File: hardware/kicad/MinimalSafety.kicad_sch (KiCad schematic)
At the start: 18 parts, among them U1 TPS3431SDRBR, U11 DRV8803PWPR, U2 SN74HCS74D, U6 SN74HCS11D

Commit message: WIP: publish current unfinished CAD sources
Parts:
- removed C1, C2, C6: 100n 16V X7R, Sirokko_TFT_Passives:C_Murata_GRM188_1608_Reflow, symbol Device:C
- removed R18, R19: 10k 1%, Resistor_SMD:R_0603_1608Metric, symbol Device:R
- removed R700, R9: 10k, Resistor_THT:R_Axial_DIN0207_L6.3mm_D2.5mm_P10.16mm_Horizontal, symbol Device:R
- removed R88: 4k7 DRV_IN3_PULLDOWN, Resistor_THT:R_Axial_DIN0207_L6.3mm_D2.5mm_P10.16mm_Horizontal, symbol Device:R
- removed R89: 10k RELAY_DRIVER_OK_PULLUP, Resistor_THT:R_Axial_DIN0207_L6.3mm_D2.5mm_P10.16mm_Horizontal, symbol Device:R
- removed U1: TPS3431SDRBR, Sirokko_Safety:TPS3431_DRB0008A_3D, symbol Sirokko_Safety:TPS3431SDRBR
- removed U2: SN74HCS74D, Package_SO:SOIC-14_3.9x8.7mm_P1.27mm, symbol Sirokko_Safety:SN74HCS74D
- removed U6: SN74HCS11D, Package_SO:SOIC-14_3.9x8.7mm_P1.27mm, symbol Sirokko_Safety:SN74HCS11D
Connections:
- net RELAY_DISABLE is gone; now on net GND: U11.8 (~{ENBL})
- net SAFETY_OK is gone; now on net MCU_PERMIT: U11.11 (IN3)
- net RELAY_DRIVER_OK: no longer names the net of U11.16 (~{FAULT})
- no-connect marks 4 -> 3
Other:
- note added: "CURRENT CONTRACT: external TPS3431 watchdog, SN74HCS74 latch and SN74HCS11 safety logic REMOVED / CANCELLED."
- note added: "DIRECT DRIVER: U11 /ENBL=GND, RESET=GND; IN1=GLOW_CMD, IN2=FUEL_CMD, IN3=MCU_PERMIT. R86/R87/R703 hold all three commands LOW during boot/reset/Hi-Z."
- note added: "FUTURE FIRMWARE REQUIREMENT (NOT IMPLEMENTED HERE): ESP32-S3 IWDT+TWDT; supervise control task; panic/reboot; keep commands OFF and prohibit automatic restart after reset."

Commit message: Publish two-relay PCB draft
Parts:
- removed R703: 10k, Resistor_THT:R_Axial_DIN0207_L6.3mm_D2.5mm_P10.16mm_Horizontal, symbol Device:R
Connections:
- net MCU_PERMIT is gone; now on net GND: U11.11 (IN3)
- net K_CLUTCH_SAFE_COIL_LOW: no longer names the net of U11.6 (OUT3)
- no-connect marks 3 -> 4
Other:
- note added: "TWO-RELAY DRIVER: IN1=GLOW_CMD; IN2=FUEL_CMD; unused IN3/IN4 and ENBL/RESET=GND. R86/R87 pull commands LOW. OUT3/OUT4 unused. No independent welded-contact cutoff. DRAFT / NO POWER / NO FLASH / NO FIRE."
- note removed: "CLEAR_N = WD_OK & RELAY_DRIVER_OK & P24_PRESENT & MCU_PERMIT"
- note removed: "DIRECT DRIVER: U11 /ENBL=GND, RESET=GND; IN1=GLOW_CMD, IN2=FUEL_CMD, IN3=MCU_PERMIT. R86/R87/R703 hold all three commands LOW during boot/reset/Hi-Z."
- note removed: "Positive ARM edge latches permission. Any CLEAR_N=0 removes permission; no automatic rearm."
- note removed: "U6.4=+3V3; no manual RESET. ARM_PULSE=GPIO41; MCU_PERMIT=GPIO21; P24_PRESENT=GPIO6 INPUT ONLY."

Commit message: Publish modular MAX31856 schematic WIP
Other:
- note removed: "Q -> safety relay IN3; /Q -> DRV8803 nENBL(8). GLOW_CMD and FUEL_CMD stay separate."
- note removed: "TPS3431 fixed WDT: 170..230ms; heartbeat falling-edge interval <=100ms. No peripheral-task heartbeat."

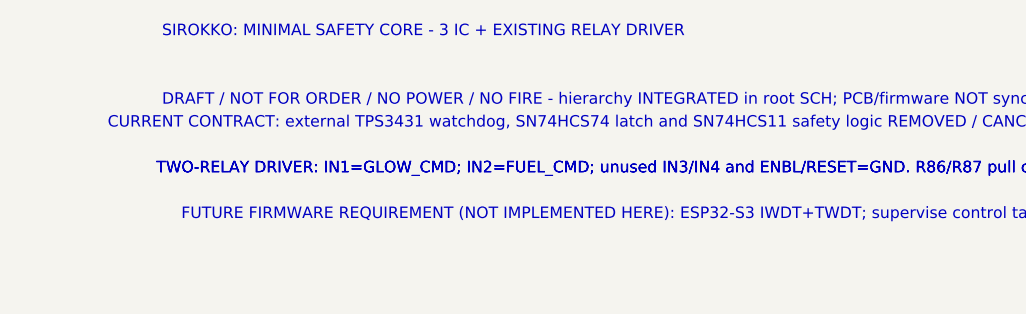
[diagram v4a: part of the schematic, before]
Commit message: Publish modular MAX31856 PCB WIP
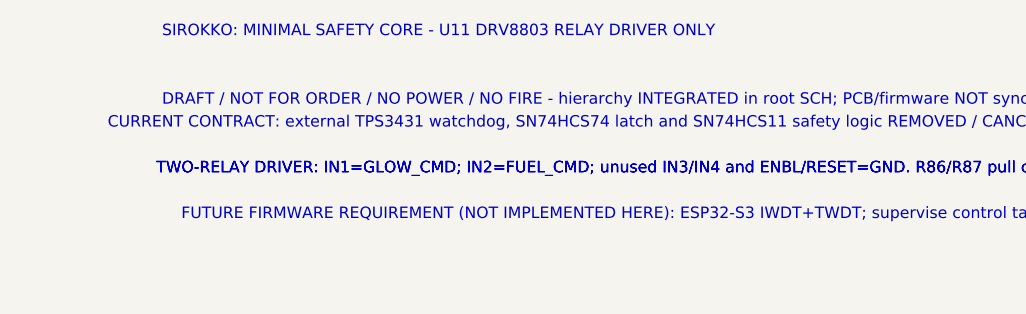
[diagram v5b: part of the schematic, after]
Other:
- note added: "SIROKKO: MINIMAL SAFETY CORE - U11 DRV8803 RELAY DRIVER ONLY"
- note removed: "SIROKKO: MINIMAL SAFETY CORE - 3 IC + EXISTING RELAY DRIVER"
